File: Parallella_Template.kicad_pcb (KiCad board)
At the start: 2 copper layers, 4 parts, among them J11 BTH-030-XX-X-D, J13 BTH-030-XX-X-D, J8 BTH-030-XX-X-D, J9 BTH-030-XX-X-D

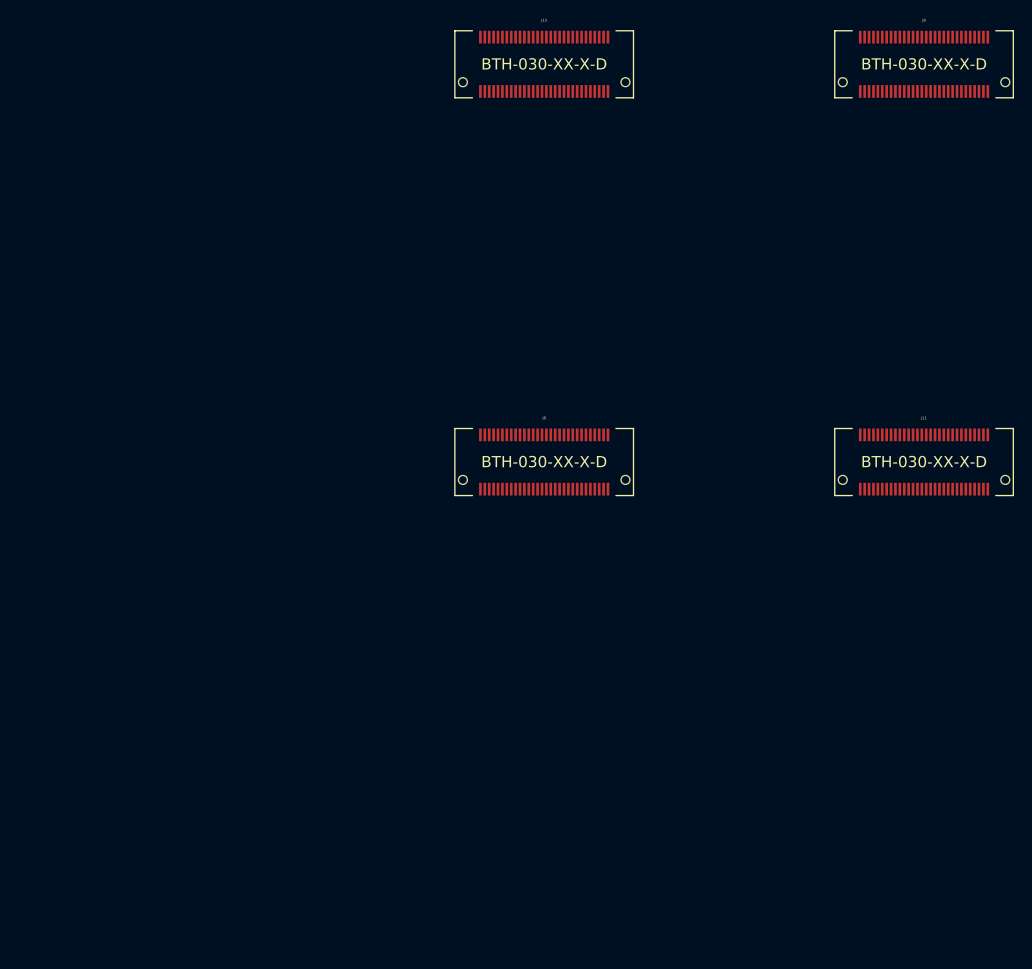
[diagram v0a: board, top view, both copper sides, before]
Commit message: Created hierarchy in schematic. Final connectors layout.
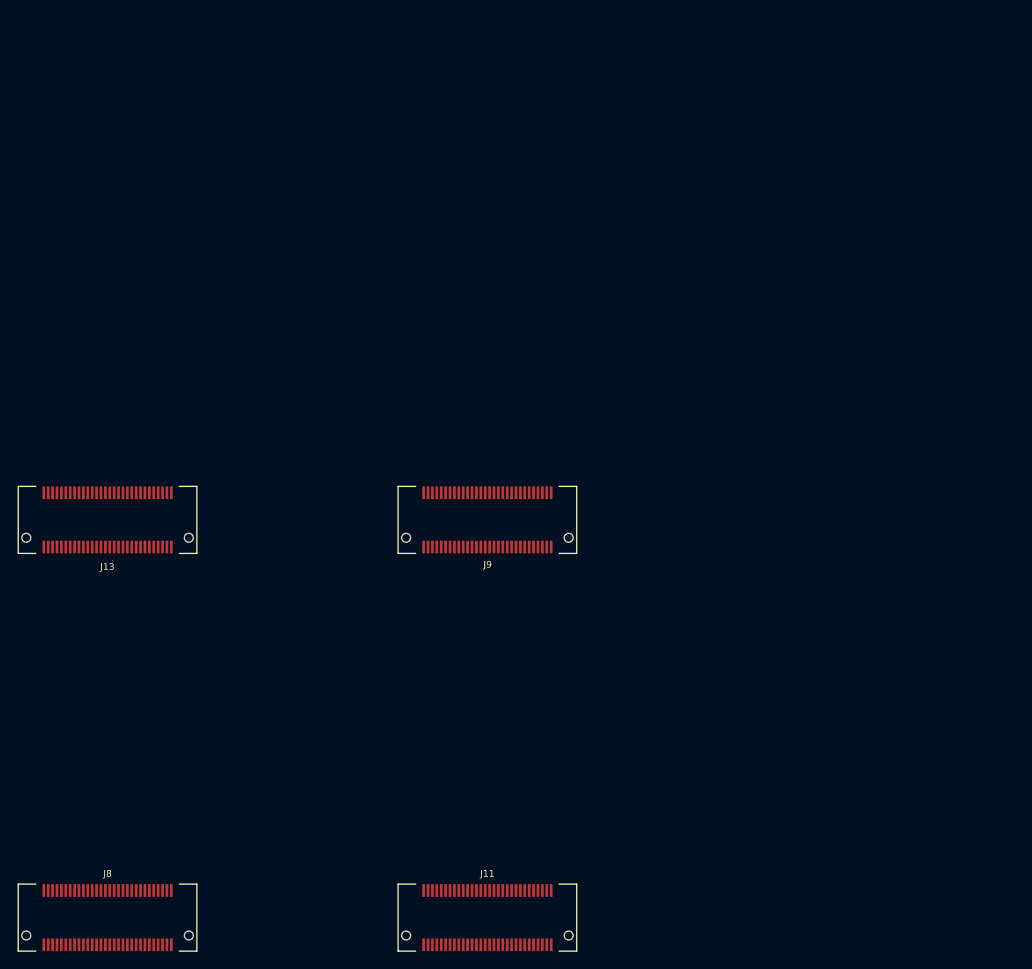
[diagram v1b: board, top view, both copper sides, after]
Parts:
- moved J11 71.7 mm to (168.1, 127.3)
- moved J8 71.7 mm to (124.9, 127.3)
- moved J9 71.7 mm to (168.1, 82.0)
- moved J13 71.7 mm to (124.9, 82.0)
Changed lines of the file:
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@@
     (links 56)
     (no_connects 56)
-    (area 105.757002 40.698156 171.656718 95.604401)
+    (area 139.776287 17.47 238.860001 80.110001)
     (thickness 1.6)
-    (drawings 4)
+    (drawings 6)
     (tracks 0)
     (zones 0)
@@
     (pad_to_mask_clearance 0)
     (aux_axis_origin 0 0)
-    (visible_elements FFFFFF7F)
+    (visible_elements 7FFFFFFF)
     (pcbplotparams
       (layerselection 3178497)
@@
   )
   (module Samtec_BTH:BTH-030-XX-X-D-A (layer F.Cu)
-    (at 174.52086 75.4634 180)
+    (at 124.88545 127.254 180)
     (descr "samtec BTH 60 pins")
     (tags "samtec, BTH, connector")
     (attr smd)
     (fp_text reference J8 (at 0 5 180) (layer F.SilkS)
-      (effects (font (size 0.29972 0.29972) (thickness 0.06096)))
-    )
-    (fp_text value BTH-030-XX-X-D (at 0 0 180) (layer F.SilkS)
+      (effects (font (size 0.762 0.762) (thickness 0.06096)))
+    )
+    (fp_text value BTH-030-XX-X-D (at 0 0 180) (layer F.SilkS) hide
       (effects (font (thickness 0.15)))
     )
@@
   )
   (module Samtec_BTH:BTH-030-XX-X-D-A (layer F.Cu)
-    (at 217.70086 30.2514 180)
+    (at 168.06545 82.042 180)
     (descr "samtec BTH 60 pins")
     (tags "samtec, BTH, connector")
     (attr smd)
-    (fp_text reference J9 (at 0 5 180) (layer F.SilkS)
-      (effects (font (size 0.29972 0.29972) (thickness 0.06096)))
-    )
-    (fp_text value BTH-030-XX-X-D (at 0 0 180) (layer F.SilkS)
+    (fp_text reference J9 (at -0.03175 -5.08 180) (layer F.SilkS)
+      (effects (font (size 0.762 0.762) (thickness 0.06096)))
+    )
+    (fp_text value BTH-030-XX-X-D (at 0 0 180) (layer F.SilkS) hide
       (effects (font (thickness 0.15)))
     )
@@
   )
   (module Samtec_BTH:BTH-030-XX-X-D-A (layer F.Cu)
-    (at 217.70086 75.4634 180)
+    (at 168.06545 127.254 180)
     (descr "samtec BTH 60 pins")
     (tags "samtec, BTH, connector")
     (attr smd)
     (fp_text reference J11 (at 0 5 180) (layer F.SilkS)
-      (effects (font (size 0.29972 0.29972) (thickness 0.06096)))
-    )
-    (fp_text value BTH-030-XX-X-D (at 0 0 180) (layer F.SilkS)
+      (effects (font (size 0.762 0.762) (thickness 0.06096)))
+    )
+    (fp_text value BTH-030-XX-X-D (at 0 0 180) (layer F.SilkS) hide
       (effects (font (thickness 0.15)))
     )
@@
   )
   (module Samtec_BTH:BTH-030-XX-X-D-A (layer F.Cu)
-    (at 174.52086 30.2514 180)
+    (at 124.88545 82.042 180)
     (descr "samtec BTH 60 pins")
     (tags "samtec, BTH, connector")
     (attr smd)
-    (fp_text reference J13 (at 0 5 180) (layer F.SilkS)
-      (effects (font (size 0.29972 0.29972) (thickness 0.06096)))
-    )
-    (fp_text value BTH-030-XX-X-D (at 0 0 180) (layer F.SilkS)
+    (fp_text reference J13 (at 0.01905 -5.334 180) (layer F.SilkS)
+      (effects (font (size 0.762 0.762) (thickness 0.06096)))
+    )
+    (fp_text value BTH-030-XX-X-D (at 0 0 180) (layer F.SilkS) hide
       (effects (font (thickness 0.15)))
     )
@@
       (net 10 3P3V))
   )
-  (gr_line (start 152.4 80.01) (end 152.4 25.4) (angle 90) (layer Dwgs.User) (width 0.2))
-  (gr_line (start 238.76 80.01) (end 152.4 80.01) (angle 90) (layer Dwgs.User) (width 0.2))
-  (gr_line (start 238.76 25.4) (end 238.76 80.01) (angle 90) (layer Dwgs.User) (width 0.2))
-  (gr_line (start 152.4 25.4) (end 238.76 25.4) (angle 90) (layer Dwgs.User) (width 0.2))
+  (dimension 54.61 (width 0.3) (layer Cmts.User)
+    (gr_text "2.1500 in" (at 96.3892 104.521 270) (layer Cmts.User)
+      (effects (font (size 1.5 1.5) (thickness 0.3)))
+    )
+    (feature1 (pts (xy 103.3272 131.826) (xy 95.0392 131.826)))
+    (feature2 (pts (xy 103.3272 77.216) (xy 95.0392 77.216)))
+    (crossbar (pts (xy 97.7392 77.216) (xy 97.7392 131.826)))
+    (arrow1a (pts (xy 97.7392 131.826) (xy 97.152779 130.699496)))
+    (arrow1b (pts (xy 97.7392 131.826) (xy 98.325621 130.699496)))
+    (arrow2a (pts (xy 97.7392 77.216) (xy 97.152779 78.342504)))
+    (arrow2b (pts (xy 97.7392 77.216) (xy 98.325621 78.342504)))
+  )
+  (dimension 86.36 (width 0.3) (layer Cmts.User)
+    (gr_text "3.4000 in" (at 146.5072 70.786) (layer Cmts.User)
+      (effects (font (size 1.5 1.5) (thickness 0.3)))
+    )
+    (feature1 (pts (xy 189.6872 77.216) (xy 189.6872 69.436)))
+    (feature2 (pts (xy 103.3272 77.216) (xy 103.3272 69.436)))
+    (crossbar (pts (xy 103.3272 72.136) (xy 189.6872 72.136)))
+    (arrow1a (pts (xy 189.6872 72.136) (xy 188.560696 72.722421)))
+    (arrow1b (pts (xy 189.6872 72.136) (xy 188.560696 71.549579)))
+    (arrow2a (pts (xy 103.3272 72.136) (xy 104.453704 72.722421)))
+    (arrow2b (pts (xy 103.3272 72.136) (xy 104.453704 71.549579)))
+  )
+  (gr_line (start 103.3272 131.826) (end 103.3272 77.216) (angle 90) (layer Dwgs.User) (width 0.2))
+  (gr_line (start 189.6872 131.826) (end 103.3272 131.826) (angle 90) (layer Dwgs.User) (width 0.2))
+  (gr_line (start 189.6872 77.216) (end 189.6872 131.826) (angle 90) (layer Dwgs.User) (width 0.2))
+  (gr_line (start 103.3272 77.216) (end 189.6872 77.216) (angle 90) (layer Dwgs.User) (width 0.2))
 )
